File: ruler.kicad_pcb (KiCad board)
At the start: 2 copper layers, 159.1 x 29.1 mm, 1 part, among them J1 Conn_01x01

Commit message: Clear out old stuff, include drawing as module
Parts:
- J1: footprint custom:pcbart -> drawing:drawing
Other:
- board size 159.1 x 29.1 mm -> 170.8 x 38.1 mm

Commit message: Do some layouting
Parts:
- added J2: USB_OTG, smisioto.eu/kicad_libs/modules/w_conn_pc.pretty:conn_usb_B_micro_smd, F.Cu at (222.7, 104.5)
- added LED1: LED TEST PADS, Tinkerforge/kicad-libraries:TESTPT, F.Cu at (103.3, 104.9)
- added LED2: 0402, KiCad/LEDs.pretty:LED_0402, F.Cu at (112.2, 108.8)
- added LED3: 0603, KiCad/LEDs.pretty:LED_0603, F.Cu at (111.8, 106.5)
- added LED4: 0805, KiCad/LEDs.pretty:LED_0805, F.Cu at (111.3, 104.5)
- added LED5: 1206, KiCad/LEDs.pretty:LED_1206, F.Cu at (110.6, 101.9)
- added R_1206: 1k, KiCad/Resistors_SMD.pretty:R_1206, F.Cu at (120.5, 101.8)
- added R_201: 1k, KiCad/Resistors_SMD.pretty:R_0201, F.Cu at (118.9, 110.9)
- added R_402: 1k, KiCad/Resistors_SMD.pretty:R_0402, F.Cu at (119.2, 108.7)
- added R_603: 1k, KiCad/Resistors_SMD.pretty:R_0603, F.Cu at (119.6, 106.4)
- added R_805: 1k, KiCad/Resistors_SMD.pretty:R_0805, F.Cu at (119.9, 104.3)
- added SW1: 6x6mm, digikey/digikey-kicad-library/digikey-footprints.pretty:Switch_Tactile_6x6mm_Vertical_SMD, F.Cu at (122.9, 77.9)
- added SW2: SW_Push, smisioto.eu/kicad_libs/modules/w_switch.pretty:smd_push2, F.Cu at (172.9, 105.0)
- added SW3: SW_Push, smisioto.eu/kicad_libs/modules/w_switch.pretty:smd_push, F.Cu at (161.5, 104.9)
- added SW4: B3U-1000P, digikey/digikey-kicad-library/digikey-footprints.pretty:Switch_Tactile_SMD_B3U-1000P, F.Cu at (132.9, 76.4)
- added SW5: SW_DPDT_x2, digikey/digikey-kicad-library/digikey-footprints.pretty:Switch_Slide_JS202011SCQN, F.Cu at (138.9, 105.3)
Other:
- board text added: "0201"
- board text added: "0402"
- board text added: "0603"
- board text added: "0805"
- board text added: "1206"
- board text added: "LED test pads"
- board text added: "LEDs"
- board text added: "Resistors"

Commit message: Add more push-buttons
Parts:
- moved SW1 66.6 mm to (184.2, 104.0)
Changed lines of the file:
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@@
   )
   (module digikey/digikey-kicad-library/digikey-footprints.pretty:Switch_Tactile_6x6mm_Vertical_SMD (layer F.Cu)
-    (at 122.905001 77.9375)
+    (at 184.22 104.04)
     (descr http://www.ckswitches.com/media/1471/pts645.pdf)
     (fp_text reference SW1 (at 0 -4.27) (layer F.SilkS)

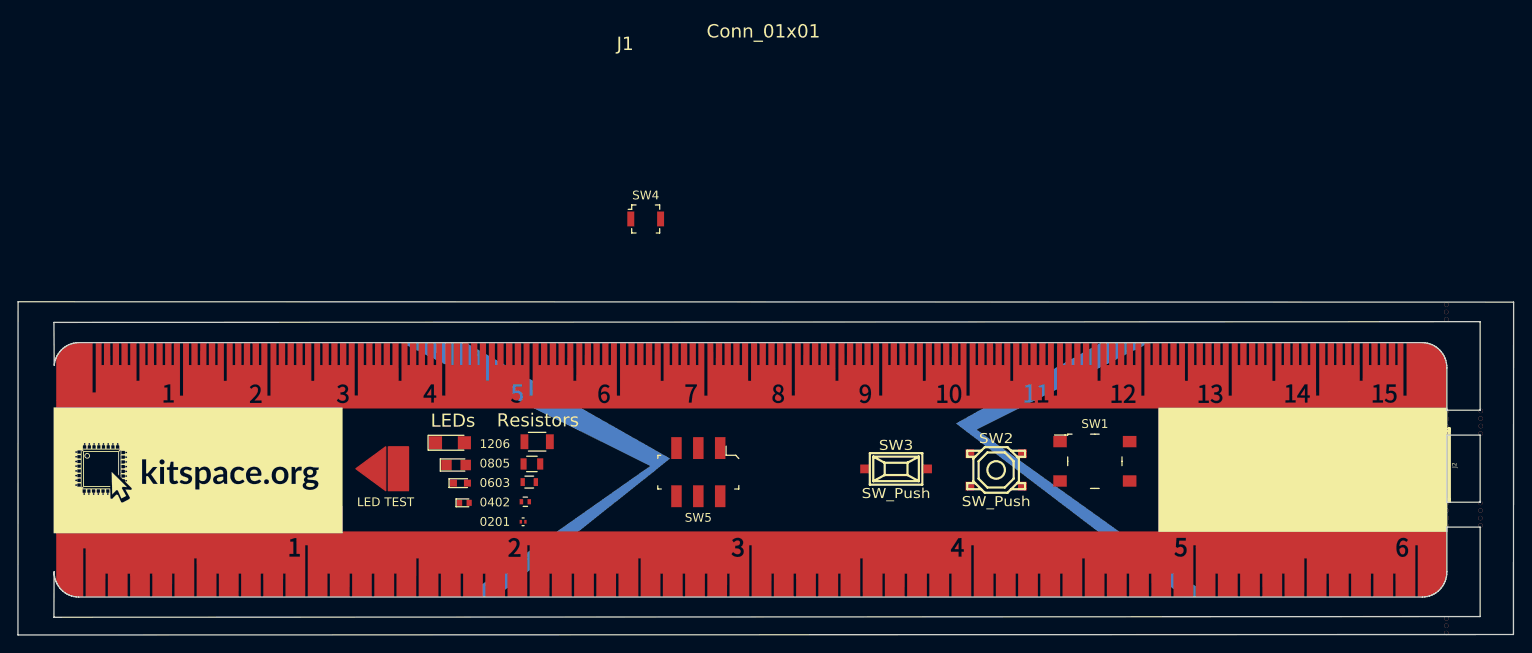
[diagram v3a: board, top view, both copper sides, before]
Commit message: Add bigger resistors
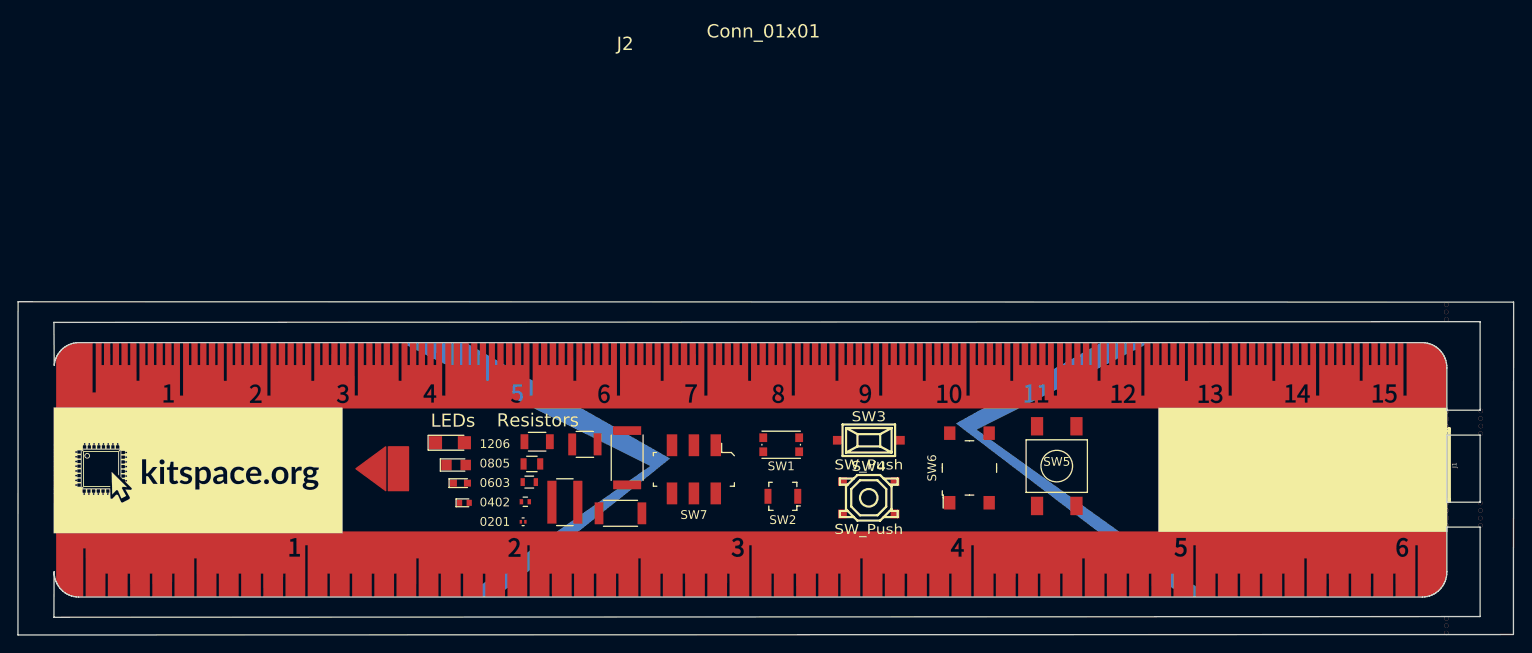
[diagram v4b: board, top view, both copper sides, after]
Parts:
- removed R_1206: 1k, KiCad/Resistors_SMD.pretty:R_1206
- added R3: 1k, KiCad/Resistors_SMD.pretty:R_1210, F.Cu at (126.0, 102.1)
- added R5: 1k, KiCad/Resistors_SMD.pretty:R_1218, F.Cu at (123.7, 108.7)
- added R7: 1k, KiCad/Resistors_SMD.pretty:R_2010, F.Cu at (130.0, 110.0)
- added R8: 1k, KiCad/Resistors_SMD.pretty:R_1206, F.Cu at (120.5, 101.8)
- added R9: 1k, KiCad/Resistors_SMD.pretty:R_2512, F.Cu at (130.8, 103.6)
- added SW1: KMR2, KiCad/Buttons_Switches_SMD.pretty:SW_SPST_KMR2, F.Cu at (148.4, 102.2)
- added SW7: SW_DPDT_x2, digikey/digikey-kicad-library/digikey-footprints.pretty:Switch_Slide_JS202011SCQN, F.Cu at (138.4, 105.0)
- LED1: footprint Tinkerforge/kicad-libraries:TESTPT -> custom:led_test_pads
- SW5: value SW_DPDT_x2 -> FSM2JSMA; footprint digikey/digikey-kicad-library/digikey-footprints.pretty:Switch_Slide_JS202011SCQN -> custom:FSM2JSMA
- moved SW5 40.9 mm to (179.9, 104.6)
- moved SW2 35.3 mm to (148.6, 108.0), turned to 180 degrees
- moved SW4 14.9 mm to (158.4, 108.2)
- moved SW6 14.3 mm to (169.9, 104.8), turned to 90 degrees
- moved SW3 4.51 mm to (158.4, 101.6)
- renumbered J2 to J1, J1 to J2, R_201 to R1, R_402 to R2, R_603 to R4, R_805 to R6, SW4 to SW2, SW2 to SW4, SW1 to SW6
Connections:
- R2 pad 1: LED_V+ -> Net-(R2-Pad1)
- R4 pad 1: LED_V+ -> Net-(R4-Pad1)
- R6 pad 1: LED_V+ -> Net-(R6-Pad1)
- SW2 pad 2: LED_V+ -> Net-(R2-Pad1)
- SW3 pad 2: LED_V+ -> Net-(R4-Pad1)
- SW4 pad 2: LED_V+ -> Net-(R4-Pad1)
- SW5 pad 1: +5V -> SW_V+
- SW5 pad 2: SW_V+ -> Net-(R6-Pad1)
- SW6 pad 2: LED_V+ -> Net-(R8-Pad1)

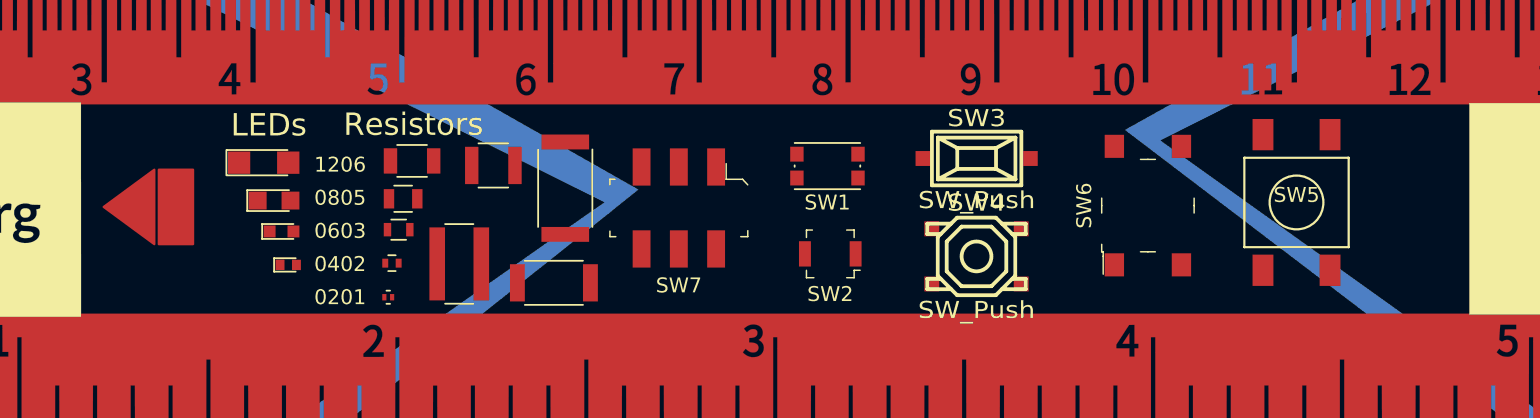
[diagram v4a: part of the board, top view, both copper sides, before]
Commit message: Add diodes
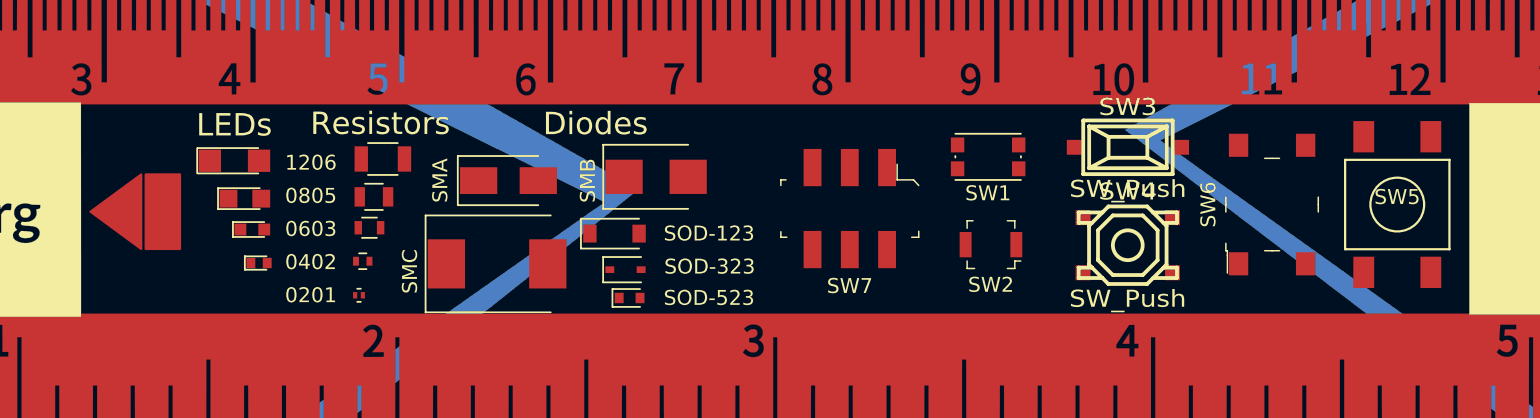
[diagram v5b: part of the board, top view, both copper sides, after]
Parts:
- removed R3: 1k, KiCad/Resistors_SMD.pretty:R_1210
- removed R5: 1k, KiCad/Resistors_SMD.pretty:R_1218
- removed R7: 1k, KiCad/Resistors_SMD.pretty:R_2010
- removed R9: 1k, KiCad/Resistors_SMD.pretty:R_2512
- added D1: SMA, KiCad/Diodes_SMD.pretty:D_SMA, F.Cu at (127.0, 103.1)
- added D2: SMB, KiCad/Diodes_SMD.pretty:D_SMB, F.Cu at (136.9, 102.9)
- added D3: SMC, KiCad/Diodes_SMD.pretty:D_SMC, F.Cu at (126.2, 108.7)
- added D4: SOD-123, KiCad/Diodes_SMD.pretty:D_SOD-123, F.Cu at (134.1, 106.7)
- added D5: SOD-323, KiCad/Diodes_SMD.pretty:D_SOD-323, F.Cu at (134.8, 109.1)
- added D6: SOD-523, KiCad/Diodes_SMD.pretty:D_SOD-523, F.Cu at (135.1, 111.0)
- moved SW7 11.5 mm to (149.9, 105.0)
- moved SW1 10.8 mm to (159.2, 101.5)
- moved SW2 10.8 mm to (159.4, 107.4)
- moved SW3 10.2 mm to (168.6, 100.9)
- moved SW4 10.2 mm to (168.6, 107.5)
- moved SW6 8.33 mm to (178.2, 104.7)
- moved SW5 6.76 mm to (186.6, 104.7)
- moved R2 1.96 mm to (117.2, 108.5)
- moved LED2 1.96 mm to (110.3, 108.7)
- moved LED3 1.96 mm to (109.8, 106.4)
- moved LED4 1.96 mm to (109.3, 104.3)
- moved R1 1.96 mm to (117.0, 110.8)
- moved R4 1.96 mm to (117.7, 106.3)
- moved R6 1.96 mm to (118.0, 104.2)
- moved LED5 1.96 mm to (108.6, 101.8)
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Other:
- board text added: "Diodes"

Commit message: Delete all routing and re-arrange
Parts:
- SW7: value SW_DPDT_x2 -> JS202011SCQN
- moved SW2 12.5 mm to (170.1, 100.9)
- moved SW3 7.39 mm to (161.2, 101.8)
- moved SW1 7.17 mm to (161.0, 108.5), turned to 0 degrees
- moved D3 1.94 mm to (128.0, 107.9)
- moved D1 1.93 mm to (128.7, 102.2)
- moved D6 1.60 mm to (136.7, 110.9)
- moved D4 1.60 mm to (135.7, 106.6)
- moved D5 1.60 mm to (136.4, 109.0)
- moved SW7 1.58 mm to (151.2, 105.9)
- moved SW4 1.30 mm to (169.8, 107.5)
- moved D2 0.30 mm to (137.2, 102.8)
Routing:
- net GND: track 0.00 -> 10.0 mm

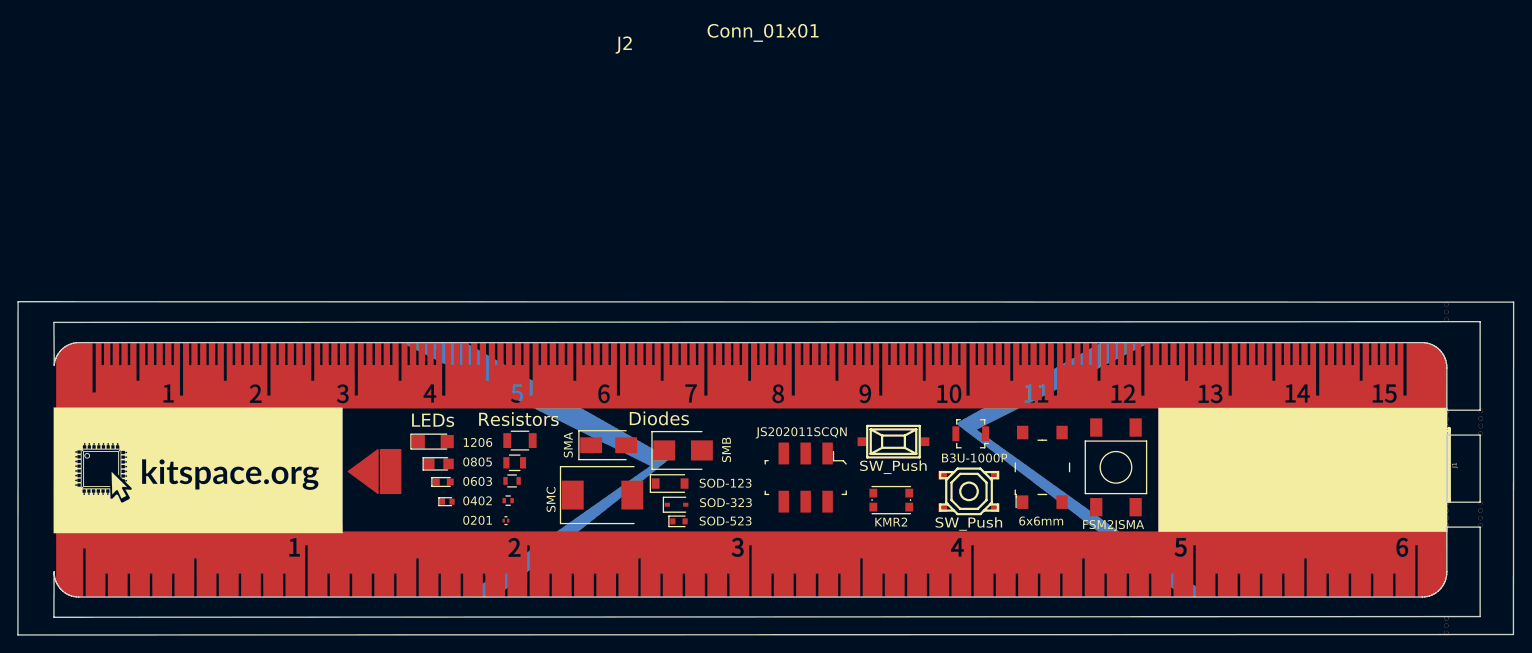
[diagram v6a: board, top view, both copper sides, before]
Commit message: Adjust mouse-bites to accommodate USB connector
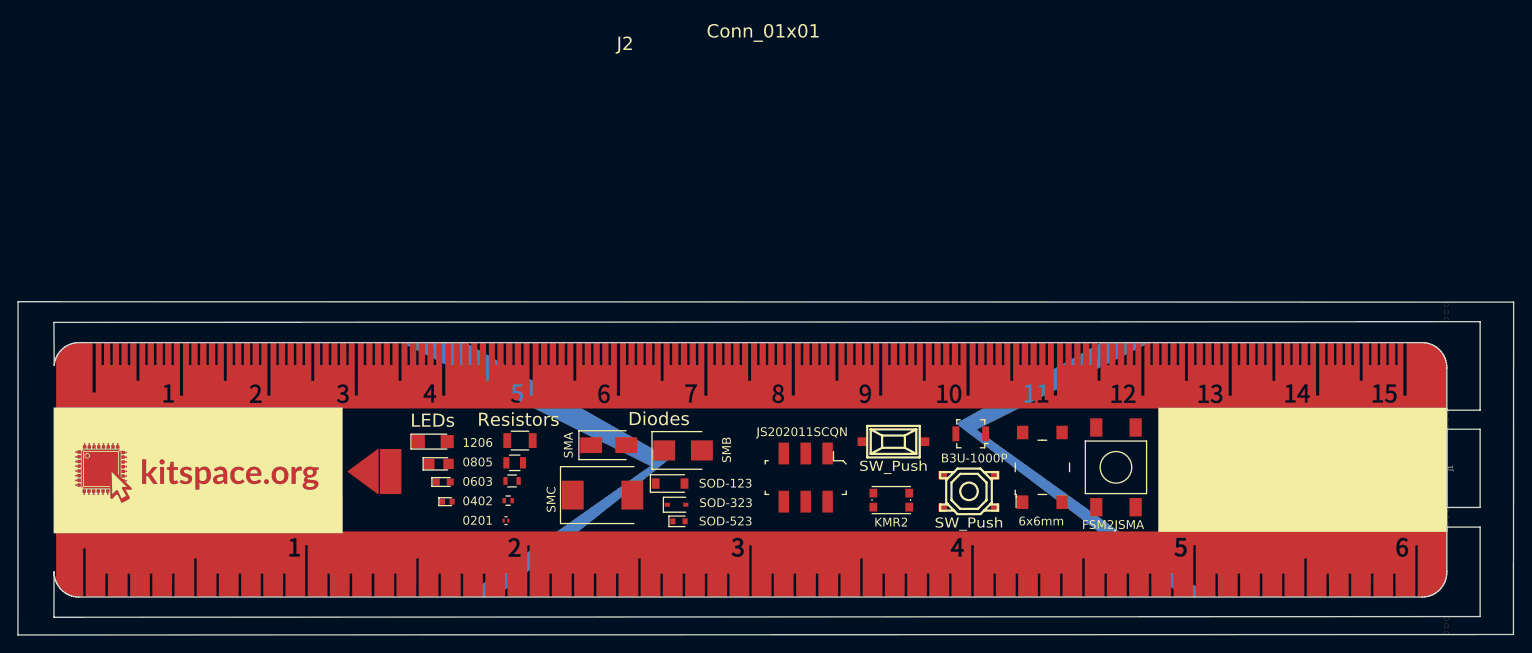
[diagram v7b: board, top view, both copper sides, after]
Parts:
- moved J1 0.54 mm to (222.2, 104.8)
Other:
- outline, holes or cut-outs redrawn

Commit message: Re-arrange push-button connections
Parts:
- renumbered R4 to R3, R6 to R4, R8 to R5, SW3 to SW2, SW2 to SW3
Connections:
- SW2 pad 2: Net-(D2-Pad1) -> Net-(D1-Pad1)
- SW3 pad 2: Net-(D1-Pad1) -> Net-(D2-Pad1)
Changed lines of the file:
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@@
     (tags "resistor 1206")
     (attr smd)
-    (fp_text reference R8 (at 0 -1.85 180) (layer F.Fab)
+    (fp_text reference R5 (at 0 -1.85 180) (layer F.Fab)
       (effects (font (size 1 1) (thickness 0.15)))
     )
@@
   (module digikey/digikey-kicad-library/digikey-footprints.pretty:Switch_Tactile_SMD_B3U-1000P (layer F.Cu)
     (at 170.05 100.9 180)
-    (fp_text reference SW2 (at 0 -2.7 180) (layer F.Fab)
+    (fp_text reference SW3 (at 0 -2.7 180) (layer F.Fab)
       (effects (font (size 1 1) (thickness 0.15)))
     )
@@
       (net 7 SW_V+))
     (pad 2 smd rect (at 1.7 0 180) (size 0.8 1.7) (layers F.Cu F.Paste F.Mask)
-      (net 17 "Net-(D1-Pad1)"))
+      (net 16 "Net-(D2-Pad1)"))
   )
   (module KiCad/Resistors_SMD.pretty:R_0201 (layer F.Cu)
@@
     (tags "resistor 0603")
     (attr smd)
-    (fp_text reference R4 (at 0 -1.45 180) (layer F.Fab)
+    (fp_text reference R3 (at 0 -1.45 180) (layer F.Fab)
       (effects (font (size 1 1) (thickness 0.15)))
     )
@@
     (tags "resistor 0805")
     (attr smd)
-    (fp_text reference R6 (at 0 -1.65 180) (layer F.Fab)
+    (fp_text reference R4 (at 0 -1.65 180) (layer F.Fab)
       (effects (font (size 1 1) (thickness 0.15)))
     )
@@
     (descr "SMD Pushbutton")
     (autoplace_cost180 10)
-    (fp_text reference SW3 (at 0 -2.70002) (layer F.Fab)
+    (fp_text reference SW2 (at 0 -2.70002) (layer F.Fab)
       (effects (font (size 1.143 1.27) (thickness 0.1524)))
     )
@@
       (net 7 SW_V+))
     (pad 2 smd rect (at 3.59918 0) (size 1.00076 1.00076) (layers F.Cu F.Paste F.Mask)
-      (net 16 "Net-(D2-Pad1)"))
+      (net 17 "Net-(D1-Pad1)"))
     (model walter/switch/smd_push.wrl
       (at (xyz 0 0 0))
